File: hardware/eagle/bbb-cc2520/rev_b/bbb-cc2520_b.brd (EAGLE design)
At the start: 54.6 x 86.4 mm, 95 parts, among them J1 TC2030-IDC, P9/P8 BBB_HEADERS, U1 CC2520, U2 CC2520, U3 CAT24C256WI-GT3, U4 CC2591, U5 CD4051B-53B, U6 NRF51822QF, X1 NX2520SA, X2 NX2520SA, X3 16MHz

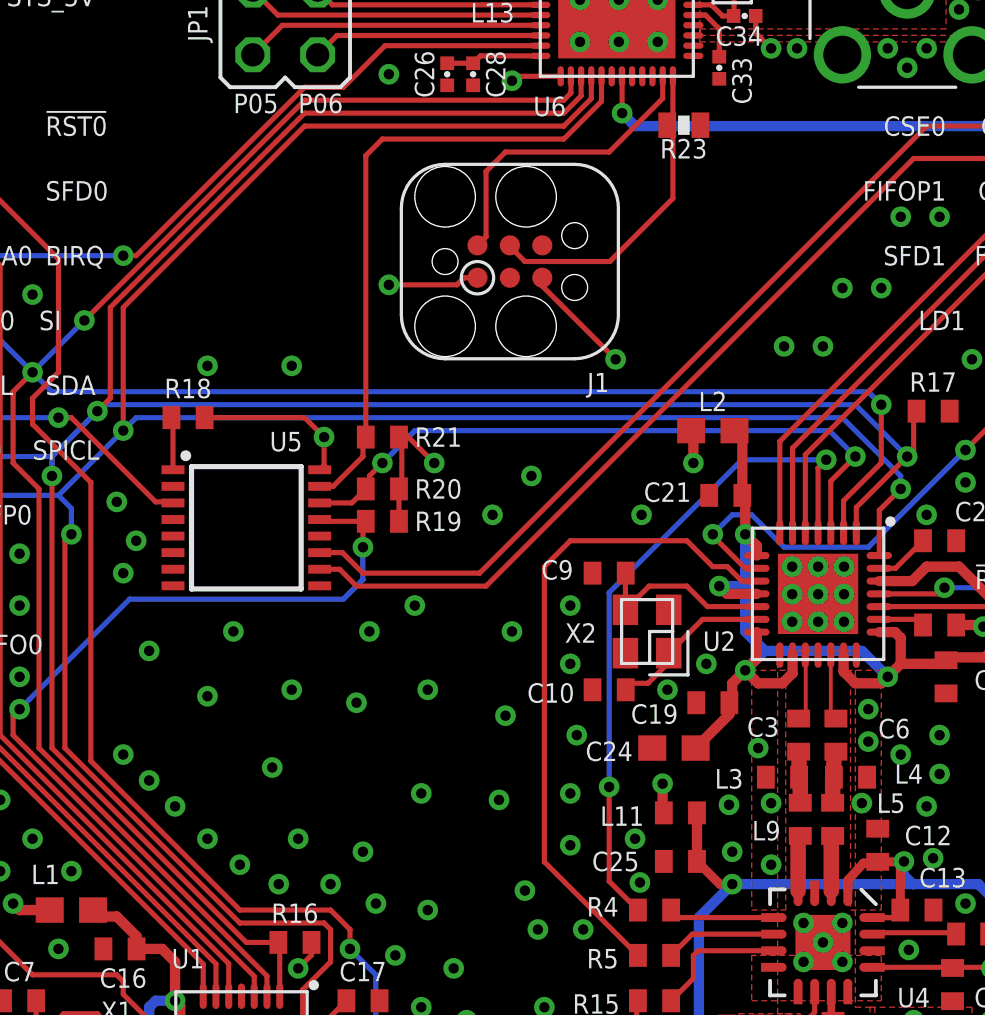
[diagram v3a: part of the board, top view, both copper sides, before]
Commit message: updated symbol for demux, added test points
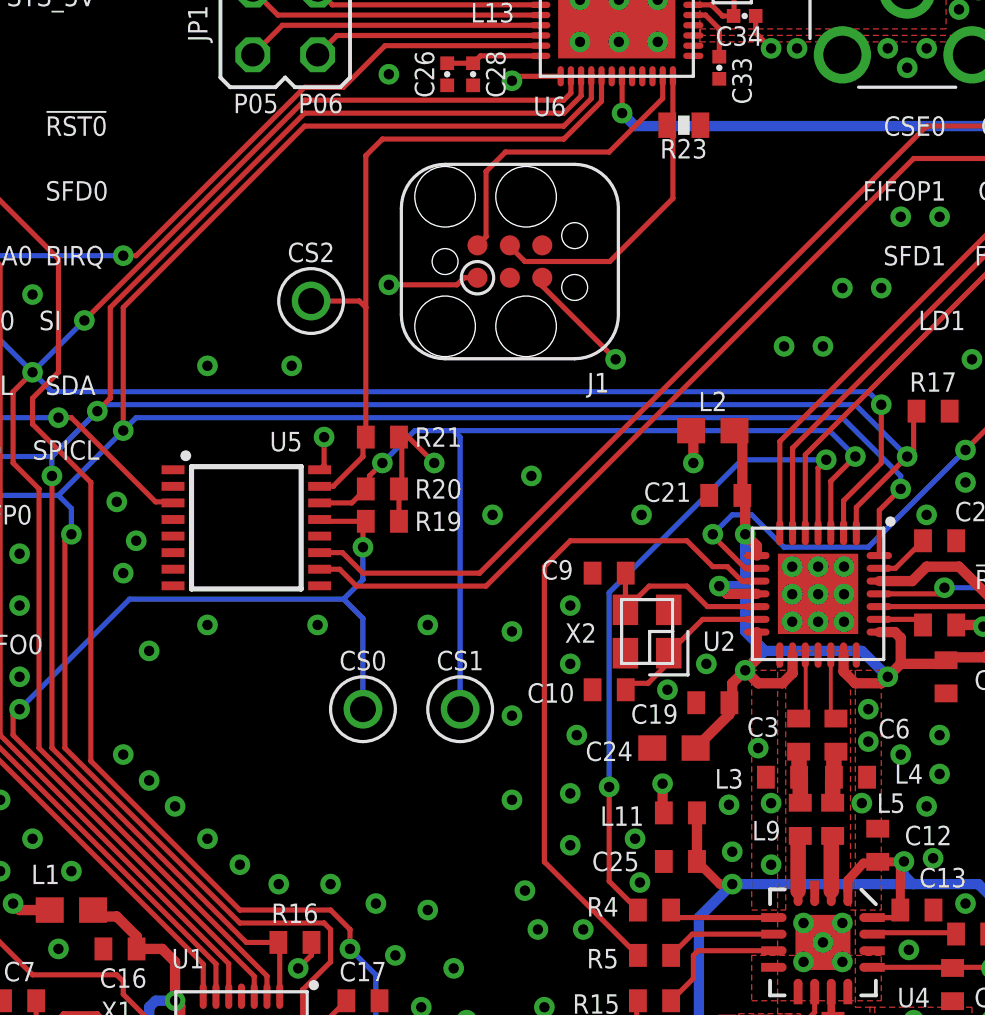
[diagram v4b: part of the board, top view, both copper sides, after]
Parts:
- removed R18: 10k 1%, rcl:R0402
- added CS0, CS1, CS2: TEST_POINT_0.040IN, headers:TESTPOINT_0.040IN
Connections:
- removed net CS3: U5.12
- removed net CS4: R18.1, U5.1
- removed net CS5: U5.5
- removed net CS6: U5.2
- removed net CS7: U5.4
- net CS0: now also CS0.TESTPOINT
- net CS1: now also CS1.TESTPOINT
- net CS2: now also CS2.TESTPOINT
- net VCC: no longer R18.2
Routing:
- net CS1: track 26.2 -> 37.2 mm
- net VCC: track 51.5 -> 46.5 mm
- net CS0: track 35.0 -> 39.6 mm
- net CS2: track 25.1 -> 27.4 mm
- net CS4: track 2.07 -> 0.00 mm
- net GND: track 21.8 -> 21.7 mm, vias 272 -> 264

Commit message: made changes to board in regards to issue 3
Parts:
- removed JP1: (no value), jumper:JP2Q
- added CS3, CS4: TPTP14SQ, testpad:TP14SQ
- added SJ2: JUMPER-PAD-2-NC_BY_TRACE, SparkFun-Passives:PAD-JUMPER-2-NC_BY_TRACE_YES_SILK
- moved D3 13.8 mm to (42.3, 66.5)
- moved R3 13.0 mm to (42.5, 65.0)
- moved R11 11.1 mm to (10.9, 63.8)
- moved C18 11.1 mm to (10.9, 66.0)
- moved R10 11.1 mm to (10.9, 61.5)
- moved R12 10.9 mm to (7.87, 69.1)
- moved R8 10.9 mm to (13.5, 63.8)
- moved R7 10.9 mm to (13.5, 66.0)
- moved R9 10.9 mm to (13.5, 61.5)
- moved SJ1 10.9 mm to (18.2, 65.9)
- moved U3 10.9 mm to (13.0, 70.4)
- moved WRT 7.58 mm to (3.68, 71.9), turned to 180 degrees
- moved R22 6.14 mm to (47.5, 65.0)
- moved D4 5.79 mm to (47.0, 66.5)
- moved D2 5.09 mm to (46.9, 71.1)
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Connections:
- removed net P04: JP1.2, U6.8
- removed net P05: JP1.4, U6.9
- removed net P06: JP1.3, U6.10
- new net !RESET2: P9/P8.P9_11, U6.8
- new net N$65: SJ2.1, U5.9
- new net N$66: CS3.TP, U5.12
- new net N$67: CS4.TP, U5.1
- new net UARTRX: P9/P8.P9_24, U6.9
- new net UARTTX: P9/P8.P9_26, U6.10
- net GND: now also SJ2.2; no longer U5.9
- net P03: no longer JP1.1
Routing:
- net UARTRX: track 0.00 -> 39.6 mm, vias 0 -> 3
- net UARTTX: track 0.00 -> 38.7 mm, vias 0 -> 3
- net !RESET2: track 0.00 -> 28.4 mm
- net SDA: track 49.0 -> 35.6 mm, vias 1 -> 2
- net P05: track 11.8 -> 0.00 mm
- net P04: track 11.7 -> 0.00 mm
- net P06: track 9.04 -> 0.00 mm
- net P03: track 8.97 -> 0.00 mm
- net N$66: track 0.00 -> 7.80 mm, vias 0 -> 2
- net SCL: track 48.2 -> 41.3 mm, vias 2 -> 0
- net N$64: track 35.0 -> 28.9 mm
- net N$67: track 0.00 -> 3.96 mm
- net VCC: track 46.5 -> 42.7 mm, vias 13 -> 12
- net N$65: track 0.00 -> 2.65 mm
- net CS0: track 39.6 -> 41.9 mm
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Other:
- board size 54.6 x 86.4 mm -> 54.6 x 73.4 mm

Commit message: cleaned up pcb
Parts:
- removed WRT: JUMPER-PTH-2-NO, SparkFun-Passives:PTH-JUMPER-2-NO_NO_SILK
- added J2: JUMPER-PTH-2-NO, SparkFun-Passives:PTH-JUMPER-2-NO_NO_SILK
- moved CS1 10.9 mm to (27.2, 40.5)
- moved CS0 9.21 mm to (13.2, 33.5)
- moved CS2 5.39 mm to (20.3, 51.8)
- moved D3 4.95 mm to (44.7, 70.9), turned to 180 degrees
- moved R2 4.79 mm to (42.7, 67.8), turned to 90 degrees
- moved D4 4.33 mm to (46.7, 70.9), turned to 180 degrees
- moved D2 4.20 mm to (42.7, 70.9), turned to 180 degrees
- moved R3 3.53 mm to (44.7, 67.8), turned to 90 degrees
- moved R22 2.90 mm to (46.7, 67.8), turned to 90 degrees
- moved R1 2.43 mm to (40.6, 67.8), turned to 90 degrees
- moved D1 1.42 mm to (40.6, 70.9), turned to 180 degrees
- moved U3 0.76 mm to (13.7, 70.4)
- moved R10 0.76 mm to (10.9, 62.2)
- moved R9 0.76 mm to (13.5, 62.2)
- moved R11 0.38 mm to (10.9, 64.1)
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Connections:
- net GND: now also J2.2; no longer D4.C, WRT.2
- net N$31: now also J2.1; no longer WRT.1
- net N$63: now also D4.C, R22.2; no longer D4.A, R22.1
- net N$64: now also R22.1; no longer R22.2
- net VCC: now also D4.A
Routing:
- net CS1: track 38.0 -> 27.3 mm
- net N$32: track 18.5 -> 14.4 mm
- net CS0: track 41.9 -> 38.0 mm
- net N$64: track 28.9 -> 31.9 mm
- net LED0: track 32.2 -> 30.6 mm
- net VCC: track 42.7 -> 43.8 mm, vias 12 -> 14
- net SCL: track 41.3 -> 42.4 mm
- net N$31: track 6.94 -> 7.65 mm
- net CS2: track 27.4 -> 26.7 mm
- net GND: vias 263 -> 265
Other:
- outline, holes or cut-outs redrawn
- board text added: "CC0-CS"
- board text added: "CC1-CS"
- board text added: "EEPROM WRITE"
- board text added: "nRF-CS"
- board text removed: "P03"
- board text removed: "P04"
- board text removed: "P05"
- board text removed: "P06"

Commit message: updated schematic
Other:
- board text added: "2014/11/20"
- board text added: "RevC"
- board text removed: "2014/09/16"
- board text removed: "REVB"
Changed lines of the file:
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@@
 <text x="51.435" y="67.564" size="1.778" layer="25" font="vector" ratio="12" align="bottom-center">P8</text>
 <text x="29.464" y="3.302" size="1.27" layer="21" font="vector" ratio="14" align="bottom-center">N.Jackson</text>
-<text x="29.464" y="2.032" size="1.016" layer="21" font="vector" ratio="12" align="bottom-center">2014/09/16</text>
+<text x="29.464" y="2.032" size="1.016" layer="21" font="vector" ratio="12" align="bottom-center">2014/11/20</text>
 <text x="29.464" y="6.604" size="1.27" layer="21" font="vector" ratio="14" align="bottom-center">ZigBeag</text>
 <text x="6.096" y="48.26" size="0.762" layer="25" font="vector" ratio="12" align="center-left">CCA0</text>
@@
 <text x="44.45" y="50.8" size="0.762" layer="25" font="vector" ratio="12" align="center-right">FIFOP1</text>
 <text x="48.26" y="43.18" size="0.762" layer="25" font="vector" ratio="12" align="center-right">LD0</text>
-<text x="29.464" y="4.826" size="1.27" layer="21" font="vector" ratio="14" align="bottom-center">REVB</text>
+<text x="29.464" y="4.826" size="1.27" layer="21" font="vector" ratio="14" align="bottom-center">RevC</text>
 <text x="9.144" y="48.26" size="0.762" layer="25" font="vector" ratio="12" align="center-left">BIRQ</text>
 <wire x1="20.955" y1="73.406" x2="0" y2="73.406" width="0" layer="20"/>

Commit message: restore rev b
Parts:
- removed CS0, CS1, CS2: TEST_POINT_0.040IN, headers:TESTPOINT_0.040IN
- removed CS3, CS4: TPTP14SQ, testpad:TP14SQ
- removed J2: JUMPER-PTH-2-NO, SparkFun-Passives:PTH-JUMPER-2-NO_NO_SILK
- removed SJ2: JUMPER-PAD-2-NC_BY_TRACE, SparkFun-Passives:PAD-JUMPER-2-NC_BY_TRACE_YES_SILK
- added JP1: (no value), jumper:JP2Q
- added R18: 10k 1%, rcl:R0402
- added WRT: JUMPER-PTH-2-NO, SparkFun-Passives:PTH-JUMPER-2-NO_NO_SILK
- moved C18 11.1 mm to (9.14, 77.0)
- moved U3 11.0 mm to (12.7, 81.3)
- moved R12 10.9 mm to (7.62, 80.0)
- moved R7 10.9 mm to (13.2, 77.0)
- moved SJ1 10.9 mm to (17.9, 76.8)
- moved R11 10.7 mm to (9.14, 74.7)
- moved R8 10.5 mm to (13.2, 74.7)
- moved R10 10.3 mm to (9.14, 72.4)
- moved R9 10.2 mm to (13.2, 72.4)
- moved R3 9.55 mm to (52.5, 73.4), turned to 0 degrees
- moved D3 9.20 mm to (52.2, 76.2), turned to 270 degrees
- moved R2 7.30 mm to (47.4, 73.4), turned to 0 degrees
- moved D2 6.94 mm to (47.1, 76.2), turned to 270 degrees
- moved R1 5.83 mm to (42.3, 73.4), turned to 0 degrees
- moved D1 5.51 mm to (42.0, 76.2), turned to 270 degrees
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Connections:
- net CSE0 renamed SPIE0
- net CSE1 renamed SPIE1
- removed net !RESET2: P9/P8.P9_11, U6.8
- removed net N$65: SJ2.1, U5.9
- removed net N$66: CS3.TP, U5.12
- removed net N$67: CS4.TP, U5.1
- removed net UARTRX: P9/P8.P9_24, U6.9
- removed net UARTTX: P9/P8.P9_26, U6.10
- new net CS3: U5.12
- new net CS4: R18.1, U5.1
- new net CS5: U5.5
- new net CS6: U5.2
- new net CS7: U5.4
- new net P04: JP1.2, U6.8
- new net P05: JP1.4, U6.9
- new net P06: JP1.3, U6.10
- net CS0: no longer CS0.TESTPOINT
- net CS1: no longer CS1.TESTPOINT
- net CS2: no longer CS2.TESTPOINT
- net GND: now also D4.C, U5.9, WRT.2; no longer J2.2, SJ2.2
- net N$31: now also WRT.1; no longer J2.1
- net N$63: now also D4.A, R22.1; no longer D4.C, R22.2
- net N$64: now also R22.2; no longer R22.1
- net P03: now also JP1.1
- net VCC: now also R18.2; no longer D4.A
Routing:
- net UARTRX: track 39.6 -> 0.00 mm, vias 3 -> 0
- net UARTTX: track 38.7 -> 0.00 mm, vias 3 -> 0
- net !RESET2: track 28.4 -> 0.00 mm
- net SDA: track 35.6 -> 49.0 mm, vias 2 -> 1
- net P05: track 0.00 -> 11.8 mm
- net P04: track 0.00 -> 11.7 mm
- net P06: track 0.00 -> 9.04 mm
- net P03: track 0.00 -> 8.97 mm
- net N$66: track 7.80 -> 0.00 mm, vias 2 -> 0
- net VCC: track 43.8 -> 51.5 mm, vias 14 -> 13
- net SCL: track 42.4 -> 48.2 mm, vias 0 -> 2
- net N$32: track 14.4 -> 18.5 mm
- net N$67: track 3.96 -> 0.00 mm
- net LED0: track 30.6 -> 33.8 mm
- net N$64: track 31.9 -> 35.0 mm
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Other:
- board size 54.6 x 73.4 mm -> 54.6 x 86.4 mm
- board text added: "2014/09/16"
- board text added: "P03"
- board text added: "P04"
- board text added: "P05"
- board text added: "P06"
- board text added: "REVB"
- board text added: "SPIE0"
- board text added: "SPIE1"
- board text removed: "2014/11/20"
- board text removed: "BIRQ"
- board text removed: "CC0-CS"
- board text removed: "CC1-CS"
- board text removed: "CSE0"
- board text removed: "CSE1"
- board text removed: "EEPROM WRITE"
- board text removed: "RevC"
- board text removed: "nRF-CS"
